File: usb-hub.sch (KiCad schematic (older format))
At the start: 16 parts, among them J1 USB_C_Receptacle_16pin, J5 USB_A socket SMT, U1 fe1-4port-hub, U2 LD1117S12TR_SOT223, Y1 12mhz 20pf

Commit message: fix some BOM values
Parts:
- J5: supplier PN Value -> UB001-2F
- U1: supplier (none) -> terminus; supplier PN (none) -> FE1.1s-BQFN24B
- U2: supplier (none) -> 低压差线性稳压器; supplier PN (none) -> HK1117C
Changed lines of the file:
@@
 F 4 "2112370" H 2550 1300 60  0001 C CNN "farnell #"
 F 5 "any/open" H 0   0   60  0001 C CNN "supplier"
-F 6 "Value" H 2550 1300 60  0001 C CNN "supplier PN"
+F 6 "UB001-2F" H 2550 1300 60  0001 C CNN "supplier PN"
 F 7 "Value" H 2550 1300 60  0001 C CNN "MOQ"
 F 8 "Value" H 2550 1300 60  0001 C CNN "leadtime"
@@
 F 2 "Housings_DFN_QFN:QFN-24-1EP_4x4mm_Pitch0.5mm" H 3800 5050 60  0001 C CNN
 F 3 "" H 3800 5050 60  0001 C CNN
+F 4 "terminus" H 0   0   60  0001 C CNN "supplier"
+F 5 "FE1.1s-BQFN24B" H 0   0   60  0001 C CNN "supplier PN"
 	1    3300 5250
 	1    0    0    -1
@@
 F 3 "http://www.st.com/st-web-ui/static/active/en/resource/technical/document/datasheet/CD00000544.pdf" H 6300 1000 50  0001 C CNN
 F 4 "1202826" H 0   0   60  0001 C CNN "farnell #"
+F 5 "低压差线性稳压器" H 0   0   60  0001 C CNN "supplier"
+F 6 "HK1117C" H 0   0   60  0001 C CNN "supplier PN"
 	1    6200 1250
 	1    0    0    -1

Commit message: differential routing, test pads
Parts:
- removed C6: 0.1uF, ceramic, 6v, 10%, x5r, Capacitors_SMD:C_0603, symbol C
- added C11: 100uf 6.3v, x5r, 20%, Capacitors_SMD:C_1206, symbol C
- added C3: 1uF, ceramic, 6v, 10%, x5r, Capacitors_SMD:C_0603, symbol C
- added L1, L2: 470R at 100M, 1A, Resistors_SMD:R_0603, symbol Ferrite_Bead
- added R11: 0R, 125mW, 1%, Resistors_SMD:R_0603, symbol R
- added TP13, TP3, TP4, TP5, TP6, TP7, TP8: TEST, fp:testpoint, symbol TEST
- C1: value 0.1uF, ceramic, 6v, 10%, x5r -> 1uF, ceramic, 6v, 10%, x5r; MOQ Value -> (none); farnell # 2522395 -> 1865556; leadtime Value -> (none); supplier PN Value -> (none)
- U2: value LD1117S12TR_SOT223 -> LY2508; footprint TO_SOT_Packages_SMD:SOT-223 -> TO_SOT_Packages_SMD:SOT-23; MOQ (none) -> Value; leadtime (none) -> Value; supplier 低压差线性稳压器 -> Liani; supplier PN HK1117C -> LY2508A33M
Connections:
- net +3V3: now also C3.1, R11.1, TP13.1
- net +5V: now also L1.1, L2.2, TP5.1; no longer J1.A4/B9 (VBUS), J1.B4/A9 (VBUS), J5.1 (VBUS)
- net Earth: now also J1.A1/B12 (GND), J1.B1/A12 (GND), J1.S1 (SHIELD), J1.S4 (SHIELD), J5.5 (Shield), C11.2, C3.2, TP8.1; no longer U1.18 (busj)
- net ext-usb_N: now also U1.9 (dm2), TP7.1; no longer U1.11 (dm1)
- net ext-usb_P: now also U1.10 (dp2), TP6.1; no longer U1.12 (dp1)
- net samd-usb_N: now also U1.11 (dm1); no longer U1.9 (dm2)
- net samd-usb_P: now also U1.12 (dp1); no longer U1.10 (dp2)
- net usb-up_N: now also TP3.1
- net usb-up_P: now also TP4.1
- new net: C11.1, J5.1 (VBUS), L1.2
- new net: J1.A4/B9 (VBUS), J1.B4/A9 (VBUS), L2.1
- new net: R11.2, U1.18 (busj)
- no-connect marks 16 -> 14
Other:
- note added: "testpoints"
- note removed: "if using a different hub, allow easy bridge from samd usb port to usb socket\n"
- moved on the sheet: C7, C8, J5, U2

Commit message: updated part numbers and specs
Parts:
- C11: farnell # 2611952 -> 2494474
- TP13, TP3, TP4, TP5, TP6, TP7, TP8: farnell # (none) -> dnp; supplier (none) -> dnp
- U2: farnell # 1202826 -> 2218573
- Y1: value 12mhz 20pf -> 12mhz +-50ppm 16-20pf; farnell # 2508794 -> 2308707
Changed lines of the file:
@@
 P 1500 5050
 F 0 "Y1" V 1454 5291 50  0000 L CNN
-F 1 "12mhz 20pf" V 1545 5291 50  0000 L CNN
+F 1 "12mhz +-50ppm 16-20pf" V 1700 4550 50  0000 L CNN
 F 2 "Crystals:Crystal_SMD_3225-4pin_3.2x2.5mm" H 1500 5050 50  0001 C CNN
 F 3 "" H 1500 5050 50  0001 C CNN
-F 4 "any/open" H 50  50  60  0001 C CNN "supplier"
-F 5 "Value" H 1500 5050 60  0001 C CNN "supplier PN"
-F 6 "Value" H 1500 5050 60  0001 C CNN "MOQ"
-F 7 "Value" H 1500 5050 60  0001 C CNN "leadtime"
-F 8 "2508794" H 0   0   60  0001 C CNN "farnell #"
+F 4 "2308707" H 0   0   60  0001 C CNN "farnell #"
+F 5 "any/open" H 50  50  60  0001 C CNN "supplier"
+F 6 "Value" H 1500 5050 60  0001 C CNN "supplier PN"
+F 7 "Value" H 1500 5050 60  0001 C CNN "MOQ"
+F 8 "Value" H 1500 5050 60  0001 C CNN "leadtime"
 	1    1500 5050
 	0    1    1    0
@@
 F 2 "TO_SOT_Packages_SMD:SOT-23" H 6400 1450 50  0001 C CNN
 F 3 "http://www.st.com/st-web-ui/static/active/en/resource/technical/document/datasheet/CD00000544.pdf" H 6500 1000 50  0001 C CNN
-F 4 "1202826" H 200 0   60  0001 C CNN "farnell #"
+F 4 "2218573" H 200 0   60  0001 C CNN "farnell #"
 F 5 "Liani" H 200 0   60  0001 C CNN "supplier"
 F 6 "LY2508A33M" H 200 0   60  0001 C CNN "supplier PN"
@@
 F 2 "Capacitors_SMD:C_1206" H 3038 1550 50  0001 C CNN
 F 3 "" H 3000 1700 50  0001 C CNN
-F 4 "2611952" H 3000 1700 60  0001 C CNN "farnell #"
+F 4 "2494474" H 3000 1700 60  0001 C CNN "farnell #"
 F 5 "Value" H 3000 1700 60  0001 C CNN "supplier"
 F 6 "Value" H 3000 1700 60  0001 C CNN "supplier PN"
@@
 F 2 "fp:testpoint" H 6850 4500 50  0001 C CNN
 F 3 "" H 6850 4500 50  0001 C CNN
+F 4 "dnp" H 0   0   60  0001 C CNN "farnell #"
+F 5 "dnp" H 0   0   60  0001 C CNN "supplier"
 	1    6850 4500
 	1    0    0    -1
@@
 F 2 "fp:testpoint" H 6850 4850 50  0001 C CNN
 F 3 "" H 6850 4850 50  0001 C CNN
+F 4 "dnp" H 0   0   60  0001 C CNN "farnell #"
+F 5 "dnp" H 0   0   60  0001 C CNN "supplier"
 	1    6850 4850
 	1    0    0    -1
@@
 F 2 "fp:testpoint" H 5550 4850 50  0001 C CNN
 F 3 "" H 5550 4850 50  0001 C CNN
+F 4 "dnp" H 0   0   60  0001 C CNN "farnell #"
+F 5 "dnp" H 0   0   60  0001 C CNN "supplier"
 	1    5550 4850
 	1    0    0    -1
@@
 F 2 "fp:testpoint" H 6300 4850 50  0001 C CNN
 F 3 "" H 6300 4850 50  0001 C CNN
+F 4 "dnp" H 0   0   60  0001 C CNN "farnell #"
+F 5 "dnp" H 0   0   60  0001 C CNN "supplier"
 	1    6300 4850
 	1    0    0    -1
@@
 F 2 "fp:testpoint" H 5550 4500 50  0001 C CNN
 F 3 "" H 5550 4500 50  0001 C CNN
+F 4 "dnp" H 0   0   60  0001 C CNN "farnell #"
+F 5 "dnp" H 0   0   60  0001 C CNN "supplier"
 	1    5550 4500
 	1    0    0    -1
@@
 F 2 "fp:testpoint" H 6300 4500 50  0001 C CNN
 F 3 "" H 6300 4500 50  0001 C CNN
+F 4 "dnp" H 0   0   60  0001 C CNN "farnell #"
+F 5 "dnp" H 0   0   60  0001 C CNN "supplier"
 	1    6300 4500
 	1    0    0    -1
@@
 F 2 "fp:testpoint" H 7450 4500 50  0001 C CNN
 F 3 "" H 7450 4500 50  0001 C CNN
+F 4 "dnp" H 0   0   60  0001 C CNN "farnell #"
+F 5 "dnp" H 0   0   60  0001 C CNN "supplier"
 	1    7450 4500
 	1    0    0    -1

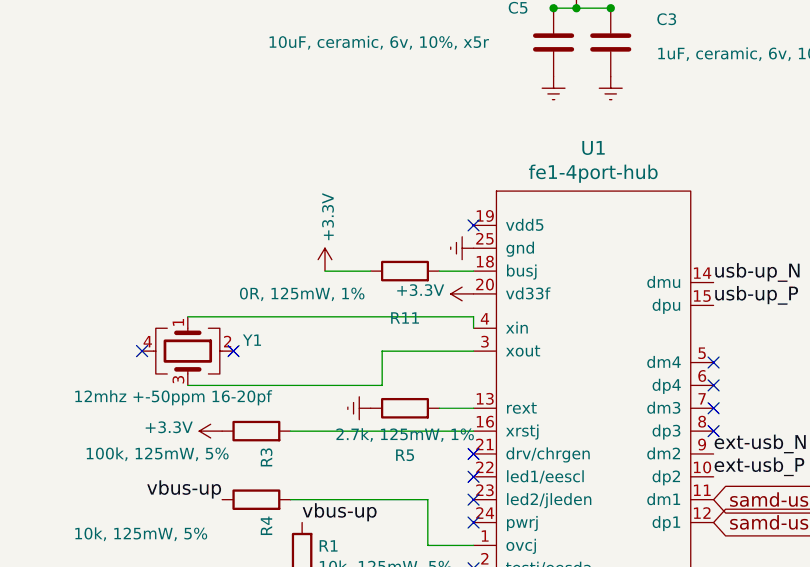
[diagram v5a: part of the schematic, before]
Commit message: remove wrong farnell partnum
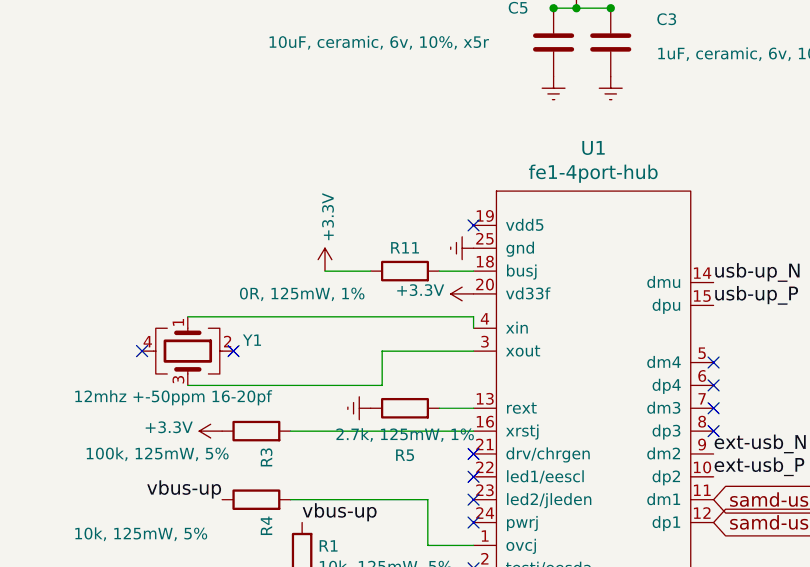
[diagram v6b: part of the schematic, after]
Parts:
- R11: farnell # 2447324 -> (none)
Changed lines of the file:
@@
 U 1 1 5AD5D031
 P 2450 4700
-F 0 "R11" V 2243 4700 50  0000 C CNN
+F 0 "R11" V 2550 4700 50  0000 C CNN
 F 1 "0R, 125mW, 1%" V 2350 5150 50  0000 C CNN
 F 2 "Resistors_SMD:R_0603" V 2380 4700 50  0001 C CNN
 F 3 "" H 2450 4700 50  0001 C CNN
-F 4 "2447324" H 0   -600 60  0001 C CNN "farnell #"
-F 5 "any/open" H -1400 300 60  0001 C CNN "supplier"
-F 6 "Value" H 2450 4700 60  0001 C CNN "supplier PN"
-F 7 "Value" H 2450 4700 60  0001 C CNN "MOQ"
-F 8 "Value" H 2450 4700 60  0001 C CNN "leadtime"
+F 4 "any/open" H -1400 300 60  0001 C CNN "supplier"
+F 5 "Value" H 2450 4700 60  0001 C CNN "supplier PN"
+F 6 "Value" H 2450 4700 60  0001 C CNN "MOQ"
+F 7 "Value" H 2450 4700 60  0001 C CNN "leadtime"
 	1    2450 4700
 	0    -1   -1   0

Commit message: footprints in submodule
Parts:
- C1, C3, C5, C7, C8: footprint Capacitors_SMD:C_0603 -> raise_fp:C_0603
- C11: footprint Capacitors_SMD:C_1206 -> raise_fp:C_1206
- J1: footprint fp:usb-c-16smt -> raise_fp:usb-c-16smt
- J5: footprint fp:usb-a-smt-bfriend -> raise_fp:usb-a-smt-bfriend
- L1, L2, R1, R11, R2, R3, R4, R5, R6: footprint Resistors_SMD:R_0603 -> raise_fp:R_0603
- TP13, TP3, TP4, TP5, TP6, TP7, TP8: footprint fp:testpoint -> raise_fp:testpoint
- U1: footprint Housings_DFN_QFN:QFN-24-1EP_4x4mm_Pitch0.5mm -> raise_fp:QFN-24-1EP_4x4mm_Pitch0.5mm
- U2: footprint TO_SOT_Packages_SMD:SOT-23 -> raise_fp:SOT-23
- Y1: footprint Crystals:Crystal_SMD_3225-4pin_3.2x2.5mm -> raise_fp:Crystal_SMD_3225-4pin_3.2x2.5mm
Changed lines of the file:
@@
 EESchema Schematic File Version 3
-LIBS:usb-hub-rescue
 LIBS:power
 LIBS:device
@@
 LIBS:contrib
 LIBS:valves
-LIBS:usb-2412
-LIBS:huble-rescue
 LIBS:rgbled
-LIBS:samd21j
-LIBS:tlv760
-LIBS:mmbzx
+LIBS:sled1735
 LIBS:usb_c_16pin
-LIBS:fe1-4port-hub
-LIBS:samd21g
-LIBS:usblc6-4
 LIBS:usb-hub-cache
 EELAYER 26 0
@@
 F 0 "J5" H 1650 2000 50  0000 C CNN
 F 1 "USB_A socket SMT" H 1900 2150 50  0000 C CNN
-F 2 "fp:usb-a-smt-bfriend" H 2050 1600 50  0001 C CNN
+F 2 "raise_fp:usb-a-smt-bfriend" H 2050 1600 50  0001 C CNN
 F 3 "" H 2050 1600 50  0001 C CNN
 F 4 "2112370" H 1900 1650 60  0001 C CNN "farnell #"
@@
 F 0 "Y1" V 1454 5291 50  0000 L CNN
 F 1 "12mhz +-50ppm 16-20pf" V 1700 4550 50  0000 L CNN
-F 2 "Crystals:Crystal_SMD_3225-4pin_3.2x2.5mm" H 1500 5050 50  0001 C CNN
+F 2 "raise_fp:Crystal_SMD_3225-4pin_3.2x2.5mm" H 1500 5050 50  0001 C CNN
 F 3 "" H 1500 5050 50  0001 C CNN
 F 4 "2308707" H 0   0   60  0001 C CNN "farnell #"
@@
 F 0 "R5" V 2243 5300 50  0000 C CNN
 F 1 "2.7k, 125mW, 1%" V 2334 5300 50  0000 C CNN
-F 2 "Resistors_SMD:R_0603" V 2380 5300 50  0001 C CNN
+F 2 "raise_fp:R_0603" V 2380 5300 50  0001 C CNN
 F 3 "" H 2450 5300 50  0001 C CNN
 F 4 "any/open" H -1400 900 60  0001 C CNN "supplier"
@@
 F 0 "C5" H 2900 3850 50  0000 L CNN
 F 1 "10uF, ceramic, 6v, 10%, x5r" H 1850 3700 50  0000 L CNN
-F 2 "Capacitors_SMD:C_0603" H 3138 3550 50  0001 C CNN
+F 2 "raise_fp:C_0603" H 3138 3550 50  0001 C CNN
 F 3 "" H 3100 3700 50  0001 C CNN
 F 4 "1288201" H -950 -1200 60  0001 C CNN "farnell #"
@@
 F 0 "R2" H 1930 6204 50  0000 R CNN
 F 1 "100k, 125mW, 5%" H 1800 6400 50  0000 R CNN
-F 2 "Resistors_SMD:R_0603" V 1930 6250 50  0001 C CNN
+F 2 "raise_fp:R_0603" V 1930 6250 50  0001 C CNN
 F 3 "" H 2000 6250 50  0001 C CNN
 F 4 "any/open" H 200 3600 60  0001 C CNN "supplier"
@@
 F 0 "R1" H 1930 5904 50  0000 R CNN
 F 1 "10k, 125mW, 5%" H 1930 5995 50  0000 R CNN
-F 2 "Resistors_SMD:R_0603" V 1930 5950 50  0001 C CNN
+F 2 "raise_fp:R_0603" V 1930 5950 50  0001 C CNN
 F 3 "" H 2000 5950 50  0001 C CNN
 F 4 "any/open" H 200 3600 60  0001 C CNN "supplier"
@@
 F 0 "R6" H 10630 2254 50  0000 R CNN
 F 1 "5.1k, 125mW, 5%" H 10630 2345 50  0000 R CNN
-F 2 "Resistors_SMD:R_0603" V 10630 2300 50  0001 C CNN
+F 2 "raise_fp:R_0603" V 10630 2300 50  0001 C CNN
 F 3 "" H 10700 2300 50  0001 C CNN
 F 4 "any/open" H 0   0   60  0001 C CNN "supplier"
@@
 F 0 "C8" H 6925 1500 50  0000 L CNN
 F 1 "10uF, ceramic, 6v, 10%, x5r" H 6925 1300 50  0000 L CNN
-F 2 "Capacitors_SMD:C_0603" H 6938 1250 30  0001 C CNN
+F 2 "raise_fp:C_0603" H 6938 1250 30  0001 C CNN
 F 3 "" H 6900 1400 60  0000 C CNN
 F 4 "1288201" H 6900 1400 60  0001 C CNN "farnell #"
@@
 F 0 "C7" H 5975 1500 50  0000 L CNN
 F 1 "10uF, ceramic, 6v, 10%, x5r" H 4700 1200 50  0000 L CNN
-F 2 "Capacitors_SMD:C_0603" H 5988 1250 30  0001 C CNN
+F 2 "raise_fp:C_0603" H 5988 1250 30  0001 C CNN
 F 3 "" H 5950 1400 60  0000 C CNN
 F 4 "1288201" H 5950 1400 60  0001 C CNN "farnell #"
@@
 F 0 "J1" H 10055 4567 50  0000 C CNN
 F 1 "USB_C_Receptacle_16pin" H 10000 4650 50  0000 C CNN
-F 2 "fp:usb-c-16smt" H 10100 3000 50  0001 C CNN
+F 2 "raise_fp:usb-c-16smt" H 10100 3000 50  0001 C CNN
 F 3 "http://www.usb.org/developers/docs/usb_31_033017.zip" H 10100 3000 50  0001 C CNN
 F 4 "contact technology corp" H 0   0   60  0001 C CNN "supplier"
@@
 F 0 "U1" H 3275 6337 60  0000 C CNN
 F 1 "fe1-4port-hub" H 3275 6231 60  0000 C CNN
-F 2 "Housings_DFN_QFN:QFN-24-1EP_4x4mm_Pitch0.5mm" H 3800 5050 60  0001 C CNN
+F 2 "raise_fp:QFN-24-1EP_4x4mm_Pitch0.5mm" H 3800 5050 60  0001 C CNN
 F 3 "" H 3800 5050 60  0001 C CNN
 F 4 "terminus" H 0   0   60  0001 C CNN "supplier"
@@
 F 0 "R3" H 1730 5354 50  0000 R CNN
 F 1 "100k, 125mW, 5%" V 1700 6150 50  0000 R CNN
-F 2 "Resistors_SMD:R_0603" V 1730 5400 50  0001 C CNN
+F 2 "raise_fp:R_0603" V 1730 5400 50  0001 C CNN
 F 3 "" H 1800 5400 50  0001 C CNN
 F 4 "any/open" H 0   2750 60  0001 C CNN "supplier"
@@
 F 0 "R4" H 1730 5654 50  0000 R CNN
 F 1 "10k, 125mW, 5%" V 1650 6500 50  0000 R CNN
-F 2 "Resistors_SMD:R_0603" V 1730 5700 50  0001 C CNN
+F 2 "raise_fp:R_0603" V 1730 5700 50  0001 C CNN
 F 3 "" H 1800 5700 50  0001 C CNN
 F 4 "any/open" H 0   3350 60  0001 C CNN "supplier"
@@
 F 0 "U2" H 6400 1492 50  0000 C CNN
 F 1 "LY2508" H 6400 1401 50  0000 C CNN
-F 2 "TO_SOT_Packages_SMD:SOT-23" H 6400 1450 50  0001 C CNN
+F 2 "raise_fp:SOT-23" H 6400 1450 50  0001 C CNN
 F 3 "http://www.st.com/st-web-ui/static/active/en/resource/technical/document/datasheet/CD00000544.pdf" H 6500 1000 50  0001 C CNN
 F 4 "2218573" H 200 0   60  0001 C CNN "farnell #"
@@
 F 0 "R11" V 2550 4700 50  0000 C CNN
 F 1 "0R, 125mW, 1%" V 2350 5150 50  0000 C CNN
-F 2 "Resistors_SMD:R_0603" V 2380 4700 50  0001 C CNN
+F 2 "raise_fp:R_0603" V 2380 4700 50  0001 C CNN
 F 3 "" H 2450 4700 50  0001 C CNN
 F 4 "any/open" H -1400 300 60  0001 C CNN "supplier"
@@
 F 0 "C3" H 3550 3800 50  0000 L CNN
 F 1 "1uF, ceramic, 6v, 10%, x5r" H 3550 3650 50  0000 L CNN
-F 2 "Capacitors_SMD:C_0603" H 3388 3550 50  0001 C CNN
+F 2 "raise_fp:C_0603" H 3388 3550 50  0001 C CNN
 F 3 "" H 3350 3700 50  0001 C CNN
 F 4 "any/open" H 1900 1050 60  0001 C CNN "supplier"
@@
 F 0 "C1" H 1765 6296 50  0000 L CNN
 F 1 "1uF, ceramic, 6v, 10%, x5r" H 550 6150 50  0000 L CNN
-F 2 "Capacitors_SMD:C_0603" H 1688 6100 50  0001 C CNN
+F 2 "raise_fp:C_0603" H 1688 6100 50  0001 C CNN
 F 3 "" H 1650 6250 50  0001 C CNN
 F 4 "any/open" H 200 3600 60  0001 C CNN "supplier"
@@
 F 0 "L1" V 3026 1450 50  0000 C CNN
 F 1 "470R at 100M, 1A" V 3150 2000 50  0000 C CNN
-F 2 "Resistors_SMD:R_0603" V 3230 1450 50  0001 C CNN
+F 2 "raise_fp:R_0603" V 3230 1450 50  0001 C CNN
 F 3 "" H 3300 1450 50  0001 C CNN
 F 4 "1515745" H 3300 1450 60  0001 C CNN "farnell #"
@@
 F 0 "L2" V 10376 1550 50  0000 C CNN
 F 1 "470R at 100M, 1A" H 10600 1100 50  0000 C CNN
-F 2 "Resistors_SMD:R_0603" V 10580 1550 50  0001 C CNN
+F 2 "raise_fp:R_0603" V 10580 1550 50  0001 C CNN
 F 3 "" H 10650 1550 50  0001 C CNN
 F 4 "1515745" H 10650 1550 60  0001 C CNN "farnell #"
@@
 F 0 "C11" H 3115 1746 50  0000 L CNN
 F 1 "100uf 6.3v, x5r, 20%" H 3115 1655 50  0000 L CNN
-F 2 "Capacitors_SMD:C_1206" H 3038 1550 50  0001 C CNN
+F 2 "raise_fp:C_1206" H 3038 1550 50  0001 C CNN
 F 3 "" H 3000 1700 50  0001 C CNN
 F 4 "2494474" H 3000 1700 60  0001 C CNN "farnell #"
@@
 F 0 "TP3" H 6928 4640 50  0000 L CNN
 F 1 "TEST" H 6928 4549 50  0000 L CNN
-F 2 "fp:testpoint" H 6850 4500 50  0001 C CNN
+F 2 "raise_fp:testpoint" H 6850 4500 50  0001 C CNN
 F 3 "" H 6850 4500 50  0001 C CNN
 F 4 "dnp" H 0   0   60  0001 C CNN "farnell #"
@@
 F 0 "TP4" H 6928 4990 50  0000 L CNN
 F 1 "TEST" H 6928 4899 50  0000 L CNN
-F 2 "fp:testpoint" H 6850 4850 50  0001 C CNN
+F 2 "raise_fp:testpoint" H 6850 4850 50  0001 C CNN
 F 3 "" H 6850 4850 50  0001 C CNN
 F 4 "dnp" H 0   0   60  0001 C CNN "farnell #"
@@
 F 0 "TP6" H 5628 4990 50  0000 L CNN
 F 1 "TEST" H 5628 4899 50  0000 L CNN
-F 2 "fp:testpoint" H 5550 4850 50  0001 C CNN
+F 2 "raise_fp:testpoint" H 5550 4850 50  0001 C CNN
 F 3 "" H 5550 4850 50  0001 C CNN
 F 4 "dnp" H 0   0   60  0001 C CNN "farnell #"
@@
 F 0 "TP7" H 6378 4990 50  0000 L CNN
 F 1 "TEST" H 6378 4899 50  0000 L CNN
-F 2 "fp:testpoint" H 6300 4850 50  0001 C CNN
+F 2 "raise_fp:testpoint" H 6300 4850 50  0001 C CNN
 F 3 "" H 6300 4850 50  0001 C CNN
 F 4 "dnp" H 0   0   60  0001 C CNN "farnell #"
@@
 F 0 "TP5" H 5628 4640 50  0000 L CNN
 F 1 "TEST" H 5628 4549 50  0000 L CNN
-F 2 "fp:testpoint" H 5550 4500 50  0001 C CNN
+F 2 "raise_fp:testpoint" H 5550 4500 50  0001 C CNN
 F 3 "" H 5550 4500 50  0001 C CNN
 F 4 "dnp" H 0   0   60  0001 C CNN "farnell #"
@@
 F 0 "TP8" H 6378 4640 50  0000 L CNN
 F 1 "TEST" H 6378 4549 50  0000 L CNN
-F 2 "fp:testpoint" H 6300 4500 50  0001 C CNN
+F 2 "raise_fp:testpoint" H 6300 4500 50  0001 C CNN
 F 3 "" H 6300 4500 50  0001 C CNN
 F 4 "dnp" H 0   0   60  0001 C CNN "farnell #"
@@
 F 0 "TP13" H 7528 4640 50  0000 L CNN
 F 1 "TEST" H 7528 4549 50  0000 L CNN
-F 2 "fp:testpoint" H 7450 4500 50  0001 C CNN
+F 2 "raise_fp:testpoint" H 7450 4500 50  0001 C CNN
 F 3 "" H 7450 4500 50  0001 C CNN
 F 4 "dnp" H 0   0   60  0001 C CNN "farnell #"
